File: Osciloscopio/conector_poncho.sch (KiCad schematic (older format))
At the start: 1 part

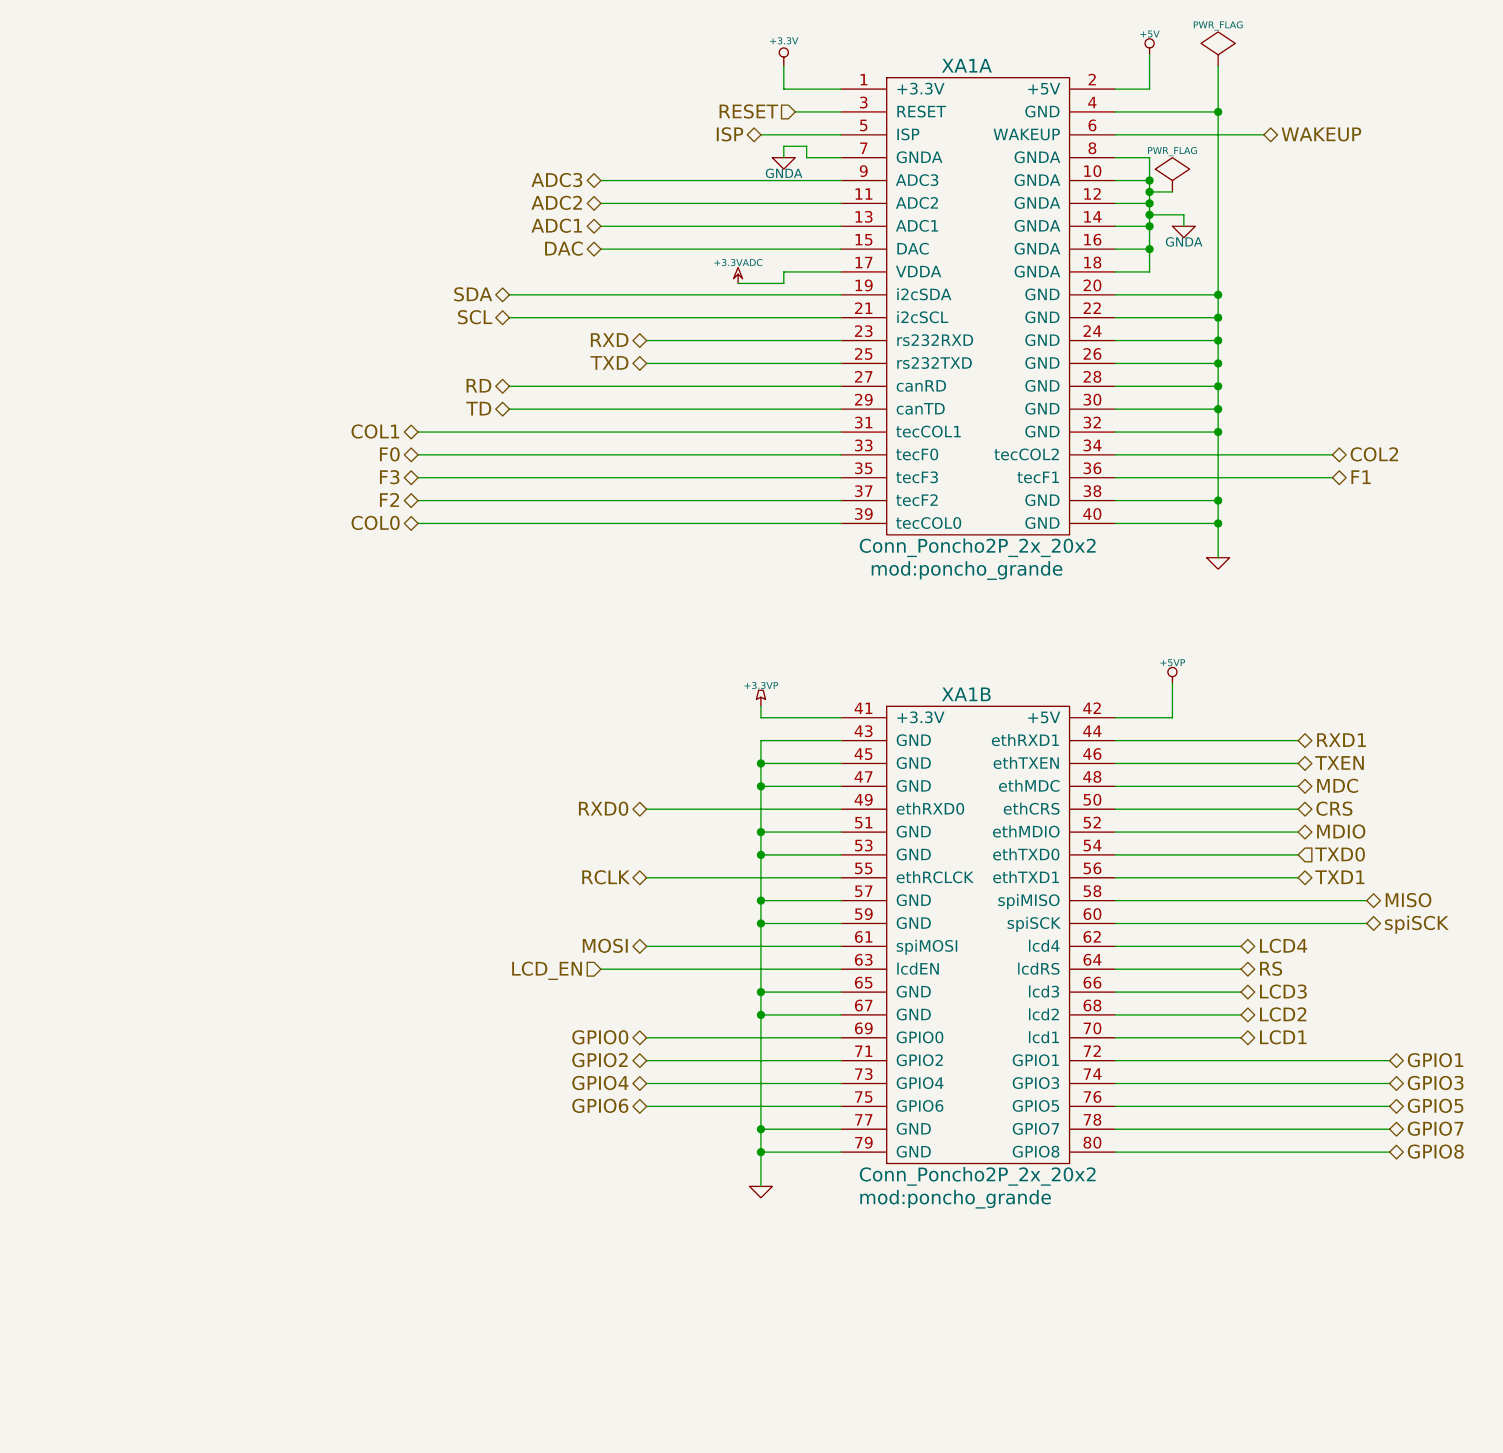
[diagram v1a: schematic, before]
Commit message: Se finaliza el prerouteo y se realizan las primeras correcciones de la revision
Este routeo cumple chequeo de DRC pero no es definitivo, le faltan planos y detalles finos.

Se realiza este commit antes de continuar con los demas cambios sugeridos por la revisión que son más peligrosos, como quitar una hoja del esquematico y quitar todos aquellos pines del AX1 que no se están utilizando
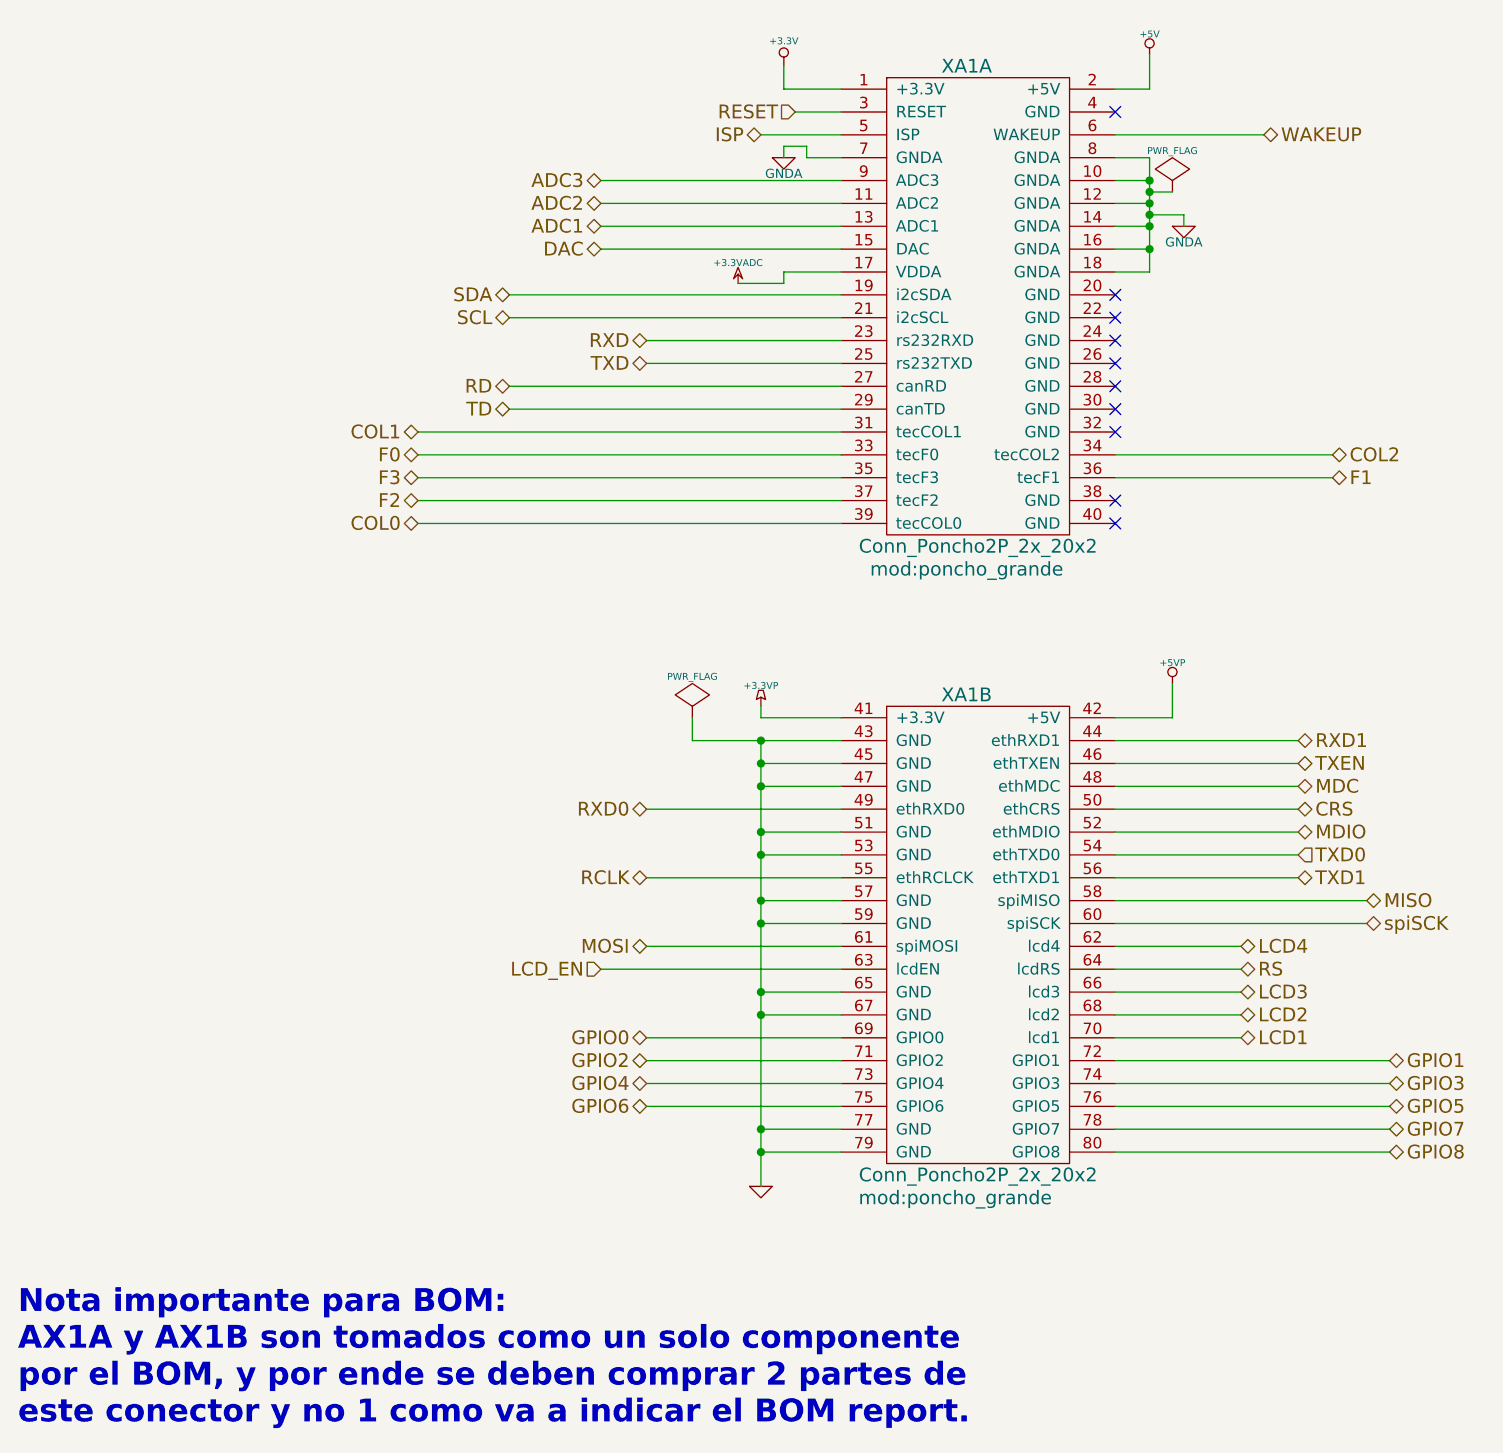
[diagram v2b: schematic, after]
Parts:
- XA1: Digikey# (none) -> S6104-ND; Manf (none) -> Sullins Connector Solutions; Manf# (none) -> PPTC202LFBN-RC
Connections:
- net GND: no longer XA1.20 (GND), XA1.22 (GND), XA1.24 (GND), XA1.26 (GND), XA1.28 (GND), XA1.30 (GND), XA1.32 (GND), XA1.38 (GND), XA1.4 (GND), XA1.40 (GND)
- no-connect marks 0 -> 10
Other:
- note added: "Nota importante para BOM: \nAX1A y AX1B son tomados como un solo componente \npor el BOM, y por ende se deben comprar 2 partes de \neste conector y no 1 como va a indicar el BOM report."
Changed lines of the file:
@@
 LIBS:power
 LIBS:conn
+LIBS:ej2cese
 LIBS:Oscilloscopio-cache
 EELAYER 25 0
@@
 Comment1 "https://github.com/ciaa/Ponchos/tree/master/modelos/doc"
 Comment2 "Autores y Licencia del template (Diego Brengi - UNLaM)"
-Comment3 "Autor del poncho Nicolás Dassieu Blanchet. Ver directorio \"doc\""
+Comment3 "Autor Nicolás Dassieu Blanchet - Curso Diseño de PCB del CESE - Ver directorio \"doc\" "
 Comment4 "CÓDIGO PONCHO:"
 $EndDescr
@@
 	5100 1500 4950 1500
 $Comp
-L GND #PWR027
-U 1 1 560A0C7E
-P 6750 3250
-F 0 "#PWR027" H 6750 3250 30  0001 C CNN
-F 1 "GND" H 6750 3180 30  0001 C CNN
-F 2 "" H 6750 3250 60  0000 C CNN
-F 3 "" H 6750 3250 60  0000 C CNN
-	1    6750 3250
-	1    0    0    -1
-$EndComp
-Wire Wire Line
-	6750 1100 6750 3250
-Wire Wire Line
-	6750 1300 6300 1300
-Wire Wire Line
-	6300 2100 6750 2100
-Connection ~ 6750 2100
-Wire Wire Line
-	6300 2200 6750 2200
-Connection ~ 6750 2200
-Wire Wire Line
-	6300 2300 6750 2300
-Connection ~ 6750 2300
-Wire Wire Line
-	6300 2400 6750 2400
-Connection ~ 6750 2400
-Wire Wire Line
-	6300 2500 6750 2500
-Connection ~ 6750 2500
-Wire Wire Line
-	6300 2600 6750 2600
-Connection ~ 6750 2600
-Wire Wire Line
-	6300 2700 6750 2700
-Connection ~ 6750 2700
-Wire Wire Line
-	6300 3000 6750 3000
-Connection ~ 6750 3000
-Wire Wire Line
-	6300 3100 6750 3100
-Connection ~ 6750 3100
-$Comp
-L GNDA #PWR028
+L GNDA #PWR027
 U 1 1 560A0D89
 P 6600 1800
-F 0 "#PWR028" H 6600 1800 40  0001 C CNN
+F 0 "#PWR027" H 6600 1800 40  0001 C CNN
 F 1 "GNDA" H 6600 1730 40  0000 C CNN
 F 2 "" H 6600 1800 60  0000 C CNN
@@
 Connection ~ 6450 1750
 $Comp
-L GND #PWR029
+L GND #PWR028
 U 1 1 560A117F
 P 4750 6000
-F 0 "#PWR029" H 4750 6000 30  0001 C CNN
+F 0 "#PWR028" H 4750 6000 30  0001 C CNN
 F 1 "GND" H 4750 5930 30  0001 C CNN
 F 2 "" H 4750 6000 60  0000 C CNN
@@
 	4750 4050 4750 6000
 Wire Wire Line
-	4750 4050 5100 4050
+	4450 4050 5100 4050
 Connection ~ 4750 5850
 Wire Wire Line
@@
 Connection ~ 4750 5750
 $Comp
-L +3.3VP #PWR030
+L +3.3VP #PWR029
 U 1 1 560A13F3
 P 4750 3900
-F 0 "#PWR030" H 4800 3930 20  0001 C CNN
+F 0 "#PWR029" H 4800 3930 20  0001 C CNN
 F 1 "+3.3VP" H 4750 3990 30  0000 C CNN
 F 2 "" H 4750 3900 60  0000 C CNN
@@
 	5100 3100 3250 3100
 $Comp
-L GNDA #PWR031
+L GNDA #PWR030
 U 1 1 560A1A14
 P 4850 1500
-F 0 "#PWR031" H 4850 1500 40  0001 C CNN
+F 0 "#PWR030" H 4850 1500 40  0001 C CNN
 F 1 "GNDA" H 4850 1430 40  0000 C CNN
 F 2 "" H 4850 1500 60  0000 C CNN
@@
 DAC
 $Comp
-L +3.3VADC #PWR032
+L +3.3VADC #PWR031
 U 1 1 560A1ACD
 P 4650 2050
-F 0 "#PWR032" H 4650 2170 20  0001 C CNN
+F 0 "#PWR031" H 4650 2170 20  0001 C CNN
 F 1 "+3.3VADC" H 4650 2140 30  0000 C CNN
 F 2 "" H 4650 2050 60  0000 C CNN
@@
 WAKEUP
 $Comp
+L PWR_FLAG #FLG032
+U 1 1 560A61E2
+P 4450 3950
+F 0 "#FLG032" H 4450 4045 30  0001 C CNN
+F 1 "PWR_FLAG" H 4450 4130 30  0000 C CNN
+F 2 "" H 4450 3950 60  0000 C CNN
+F 3 "" H 4450 3950 60  0000 C CNN
+	1    4450 3950
+	1    0    0    -1
+$EndComp
+$Comp
 L PWR_FLAG #FLG033
-U 1 1 560A61E2
-P 6750 1100
-F 0 "#FLG033" H 6750 1195 30  0001 C CNN
-F 1 "PWR_FLAG" H 6750 1280 30  0000 C CNN
-F 2 "" H 6750 1100 60  0000 C CNN
-F 3 "" H 6750 1100 60  0000 C CNN
-	1    6750 1100
-	1    0    0    -1
-$EndComp
-$Comp
-L PWR_FLAG #FLG034
 U 1 1 560A61F6
 P 6550 1650
-F 0 "#FLG034" H 6550 1745 30  0001 C CNN
+F 0 "#FLG033" H 6550 1745 30  0001 C CNN
 F 1 "PWR_FLAG" H 6550 1830 30  0000 C CNN
 F 2 "" H 6550 1650 60  0000 C CNN
@@
 	1    0    0    -1
 $EndComp
-Connection ~ 6750 1300
 Wire Wire Line
 	6550 1650 6450 1650
@@
 	6450 1200 6300 1200
 $Comp
-L +5V #PWR035
+L +5V #PWR034
 U 1 1 560C551F
 P 6450 1050
-F 0 "#PWR035" H 6450 1140 20  0001 C CNN
+F 0 "#PWR034" H 6450 1140 20  0001 C CNN
 F 1 "+5V" H 6450 1140 30  0000 C CNN
 F 2 "" H 6450 1050 60  0000 C CNN
@@
 	6550 3950 6300 3950
 $Comp
-L +5VP #PWR036
+L +5VP #PWR035
 U 1 1 560CBF57
 P 6550 3800
-F 0 "#PWR036" H 6550 3890 20  0001 C CNN
+F 0 "#PWR035" H 6550 3890 20  0001 C CNN
 F 1 "+5VP" H 6550 3890 30  0000 C CNN
 F 2 "" H 6550 3800 60  0000 C CNN
@@
 F 2 "mod:poncho_grande" H 5600 2450 60  0000 C CNN
 F 3 "" H 5350 4250 60  0000 C CNN
+F 4 "S6104-ND" H 5350 4250 60  0001 C CNN "Digikey#"
+F 5 "PPTC202LFBN-RC" H 5350 4250 60  0001 C CNN "Manf#"
+F 6 "Sullins Connector Solutions" H 5350 4250 60  0001 C CNN "Manf"
 	2    5350 4250
 	1    0    0    -1
@@
 F 2 "mod:poncho_grande" H 5650 -300 60  0000 C CNN
 F 3 "" H 5350 1500 60  0000 C CNN
+F 4 "S6104-ND" H 5350 1500 60  0001 C CNN "Digikey#"
+F 5 "PPTC202LFBN-RC" H 5350 1500 60  0001 C CNN "Manf#"
+F 6 "Sullins Connector Solutions" H 5350 1500 60  0001 C CNN "Manf"
 	1    5350 1500
 	1    0    0    -1
 $EndComp
+Text Notes 1500 7050 0    100  ~ 20
+Nota importante para BOM: \nAX1A y AX1B son tomados como un solo componente \npor el BOM, y por ende se deben comprar 2 partes de \neste conector y no 1 como va a indicar el BOM report.
+Wire Wire Line
+	4450 4050 4450 3950
+Connection ~ 4750 4050
+NoConn ~ 6300 2100
+NoConn ~ 6300 2200
+NoConn ~ 6300 2300
+NoConn ~ 6300 2400
+NoConn ~ 6300 2500
+NoConn ~ 6300 2600
+NoConn ~ 6300 2700
+NoConn ~ 6300 3000
+NoConn ~ 6300 3100
+NoConn ~ 6300 1300
 $EndSCHEMATC
